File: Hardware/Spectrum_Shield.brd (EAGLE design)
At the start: 59.7 x 53.3 mm, 25 parts, among them IC1 MSGEQ7SOIC, IC2 MSGEQ7SOIC, U1 ARDUINO_R3_SHIELD

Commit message: computer change #2
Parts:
- removed JP1: LOGO-SFENEW, SparkFun:SFE-NEW-WEBLOGO
- added U$2: (no value), SparkFun-Aesthetics:SFE_LOGO_FLAME_.2
- C1, C2, C3, C4: device SparkFun:0402-CAP -> SparkFun-Capacitors:0603-CAP
- moved U$1 66.8 mm to (57.0, 8.13)
- moved JP5 31.9 mm to (57.1, 38.1)
- moved C5 8.98 mm to (44.5, 22.9), turned to 270 degrees
- moved IC2 7.62 mm to (35.6, 17.5)
- moved C6 6.48 mm to (41.9, 34.3), turned to 180 degrees
- moved IC1 5.68 mm to (35.6, 34.3)
- moved S1 5.60 mm to (47.9, 9.14)
- moved C2 5.55 mm to (36.6, 40.6)
- moved C8 5.39 mm to (33.0, 40.6)
- moved C3 5.19 mm to (41.9, 13.1)
- moved C7 5.09 mm to (34.5, 24.3)
- moved R2 5.04 mm to (34.8, 40.6)
- moved C1 5.04 mm to (41.9, 32.3)
- moved C4 4.95 mm to (38.5, 24.3)
- moved R1 4.30 mm to (36.6, 24.3)
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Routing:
- net VCC: track 25.1 -> 56.9 mm
- net ANALOG0: track 15.2 -> 38.2 mm, vias 2 -> 3
- net RIGHT: track 29.3 -> 45.8 mm
- net LEFT: track 16.7 -> 31.3 mm, vias 1 -> 0
- net RESET: track 37.7 -> 45.3 mm
- net N$5: track 4.43 -> 9.77 mm
- net STROBE: track 40.9 -> 45.6 mm
- net N$4: track 7.93 -> 12.2 mm
- net N$3: track 7.97 -> 11.2 mm
- net N$2: track 2.13 -> 5.24 mm
- net N$227: track 23.0 -> 25.8 mm
- net ANALOG1: track 19.1 -> 20.9 mm
- net N$6: track 4.64 -> 3.15 mm
- net N$1: track 2.13 -> 2.96 mm
- net N$7: track 1.57 -> 2.34 mm
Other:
- board text removed: "Spectrum Shield"

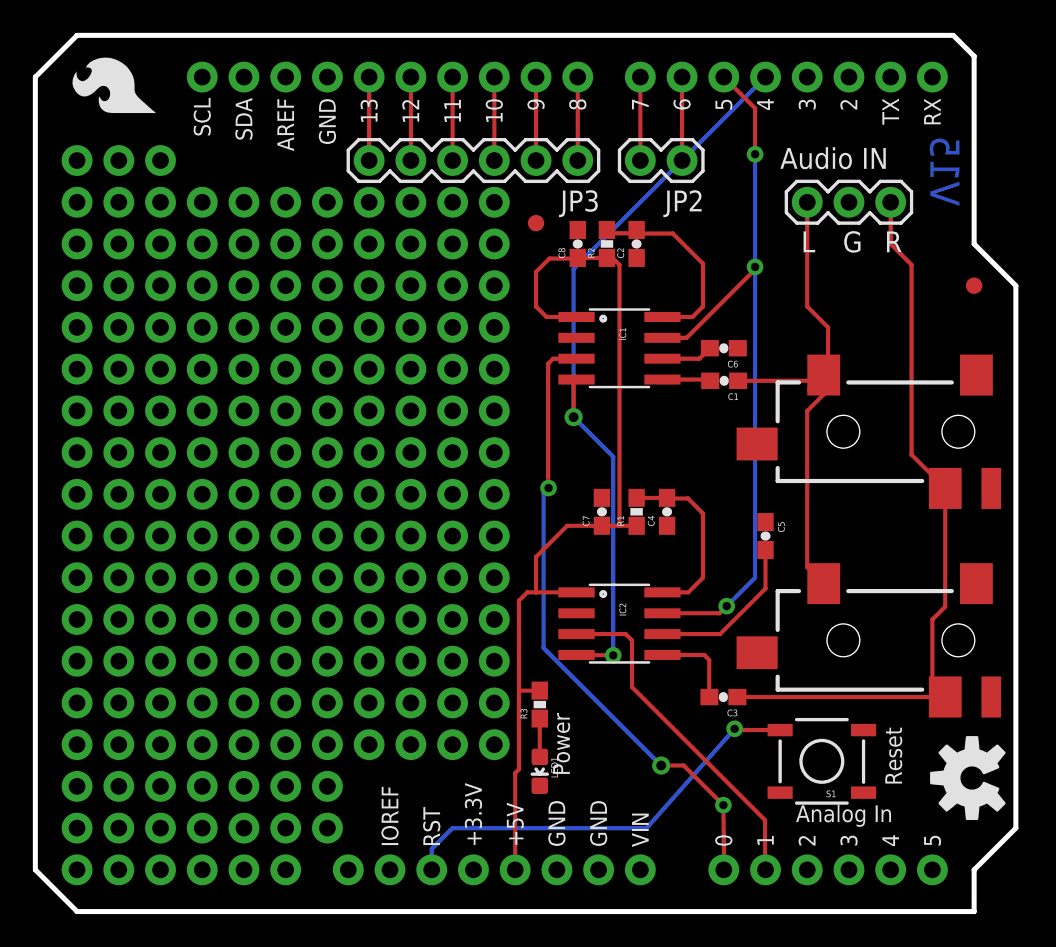
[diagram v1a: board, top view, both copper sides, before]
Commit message: Upd audiojk/0603/ trace re-routes
Updated the audio jack to smd, changed res/caps to 0603 as well as the
LED.  Added the OSHW logo and updated the shield to the R3.
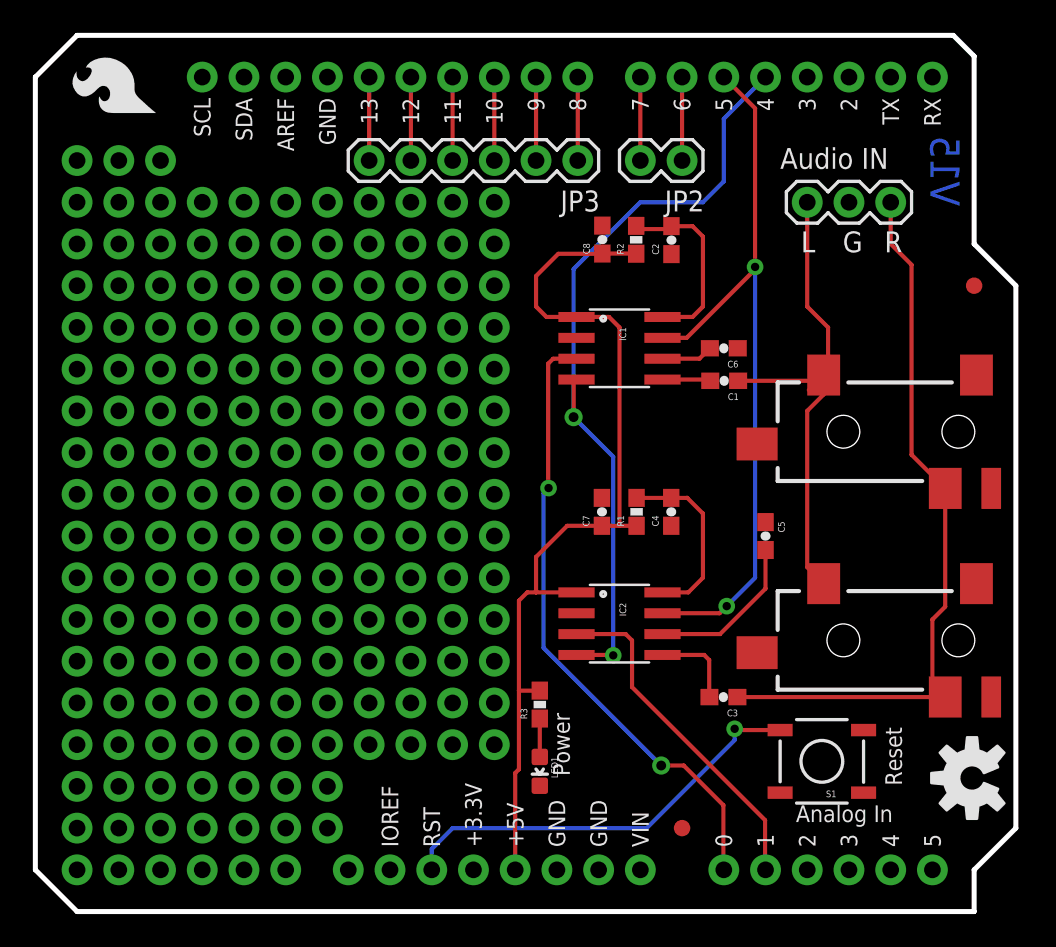
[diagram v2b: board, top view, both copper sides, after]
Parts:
- moved JP4 37.9 mm to (39.4, 5.08)
- moved C2 2.14 mm to (38.7, 40.9)
- moved R2 1.80 mm to (36.6, 40.9)
- moved C8 1.52 mm to (34.5, 40.9)
- moved C4 0.25 mm to (38.7, 24.3)
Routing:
- net STROBE: track 45.6 -> 47.9 mm
- net N$4: track 12.2 -> 11.5 mm
- net ANALOG0: track 38.2 -> 38.1 mm, vias 3 -> 2
- net RESET: vias 3 -> 2

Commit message: Trace Clean up.
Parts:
- moved JP4 17.3 mm to (56.6, 4.70)
- moved R3 2.59 mm to (33.2, 12.1)
- moved LED1 2.57 mm to (33.2, 8.92)
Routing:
- net STROBE: track 47.9 -> 45.6 mm
- net VCC: track 56.7 -> 58.0 mm
- net N$7: track 2.34 -> 1.45 mm
- net ANALOG0: track 38.1 -> 37.3 mm
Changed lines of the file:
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@@
 <setting verticaltext="up"/>
 </settings>
-<grid distance="0.05" unitdist="inch" unit="inch" style="lines" multiple="1" display="yes" altdistance="0.0001" altunitdist="inch" altunit="inch"/>
+<grid distance="0.05" unitdist="inch" unit="inch" style="lines" multiple="1" display="yes" altdistance="0.005" altunitdist="inch" altunit="inch"/>
 <layers>
 <layer number="1" name="Top" color="4" fill="1" visible="yes" active="yes"/>
@@
 <layer number="47" name="Measures" color="7" fill="1" visible="no" active="yes"/>
 <layer number="48" name="Document" color="7" fill="1" visible="no" active="yes"/>
-<layer number="49" name="Reference" color="7" fill="1" visible="yes" active="yes"/>
+<layer number="49" name="Reference" color="7" fill="1" visible="no" active="yes"/>
 <layer number="50" name="dxf" color="7" fill="1" visible="no" active="yes"/>
 <layer number="51" name="tDocu" color="6" fill="1" visible="yes" active="yes"/>
@@
 <wire x1="0" y1="2.54" x2="2.54" y2="0" width="0.3048" layer="20"/>
 <text x="33.274" y="40.386" size="2.1844" layer="22" font="vector" ratio="15" rot="MR270">bliptronics.com</text>
-<text x="35.179" y="37.211" size="1.27" layer="22" font="vector" ratio="15" rot="MR270">Based on design by</text>
+<text x="35.814" y="36.83" size="1.27" layer="22" font="vector" ratio="15" rot="MR270">Based on design by</text>
 <text x="45.339" y="45.212" size="1.27" layer="21" font="vector" ratio="15">Audio IN</text>
 <text x="46.609" y="40.132" size="1.27" layer="21" font="vector" ratio="15">L</text>
@@
 <text x="51.689" y="40.132" size="1.27" layer="21" font="vector" ratio="15">R</text>
 <text x="51.7398" y="11.2268" size="1.016" layer="21" font="vector" ratio="15" rot="R270">Reset</text>
-<text x="32.5374" y="8.255" size="1.016" layer="21" font="vector" ratio="15" rot="R90">Power</text>
-<text x="56.261" y="47.244" size="1.778" layer="16" font="vector" ratio="15" rot="MR270">V15</text>
+<text x="35.0774" y="8.255" size="1.016" layer="21" font="vector" ratio="15" rot="R90">Power</text>
+<text x="56.261" y="47.244" size="1.27" layer="16" font="vector" ratio="15" rot="MR270">V15</text>
 </plain>
 <attributes>
@@
 <element name="AUDIO_IN" library="SparkFun" package="1X03" value="JUMPER-3PTH" x="46.99" y="43.18" smashed="yes"/>
 <element name="U1" library="SparkFun-Boards" package="UNO_R3_SHIELD" value="ARDUINO_R3_SHIELD" x="0" y="53.34" rot="R270"/>
-<element name="R3" library="SparkFun-Resistors" package="0603-RES" value="330" x="30.7086" y="12.5984" rot="R90">
-<attribute name="PROD_ID" value="RES-00818" x="30.7086" y="12.5984" size="1.778" layer="27" rot="R90" display="off"/>
-<attribute name="VALUE" value="330" x="30.7086" y="12.5984" size="1.778" layer="27" rot="R90" display="off"/>
-</element>
-<element name="LED1" library="SparkFun-LED" package="LED-0603" value="RED" x="30.7086" y="8.5344" rot="R180">
-<attribute name="PROD_ID" value="DIO-00819" x="30.7086" y="8.5344" size="1.778" layer="27" rot="R180" display="off"/>
-<attribute name="VALUE" value="RED" x="30.7086" y="8.5344" size="1.778" layer="27" rot="R180" display="off"/>
+<element name="R3" library="SparkFun-Resistors" package="0603-RES" value="330" x="33.2486" y="12.0904" rot="R90">
+<attribute name="PROD_ID" value="RES-00818" x="33.2486" y="12.0904" size="1.778" layer="27" rot="R90" display="off"/>
+<attribute name="VALUE" value="330" x="33.2486" y="12.0904" size="1.778" layer="27" rot="R90" display="off"/>
+</element>
+<element name="LED1" library="SparkFun-LED" package="LED-0603" value="RED" x="33.2486" y="8.9154" rot="R180">
+<attribute name="PROD_ID" value="DIO-00819" x="33.2486" y="8.9154" size="1.778" layer="27" rot="R180" display="off"/>
+<attribute name="VALUE" value="RED" x="33.2486" y="8.9154" size="1.778" layer="27" rot="R180" display="off"/>
 </element>
 <element name="JP2" library="SparkFun" package="1X02" value="" x="39.37" y="45.72" rot="R180"/>
@@
 <element name="IC1" library="SparkFun" package="SOIC8" value="MSGEQ7SOIC" x="35.56" y="34.29" rot="R270"/>
 <element name="IC2" library="SparkFun" package="SOIC8" value="MSGEQ7SOIC" x="35.56" y="17.526" rot="R270"/>
-<element name="JP4" library="SparkFun" package="FIDUCIAL-1X2" value="FIDUCIAL1X2" x="39.37" y="5.08"/>
+<element name="JP4" library="SparkFun" package="FIDUCIAL-1X2" value="FIDUCIAL1X2" x="56.642" y="4.699"/>
 <element name="JP5" library="SparkFun" package="FIDUCIAL-1X2" value="FIDUCIAL1X2" x="57.15" y="38.1"/>
 <element name="U$1" library="SparkFun-Aesthetics" package="OSHW-LOGO-M" value="" x="57.023" y="8.128" rot="R90"/>
@@
 <wire x1="32.766" y1="30.099" x2="32.766" y2="32.2072" width="0.254" layer="1"/>
 <wire x1="32.766" y1="32.2072" x2="32.9438" y2="32.385" width="0.254" layer="1"/>
-<wire x1="32.766" y1="39.116" x2="32.766" y2="30.099" width="0.254" layer="16"/>
 <wire x1="32.766" y1="30.099" x2="35.179" y2="27.686" width="0.254" layer="16"/>
 <wire x1="35.179" y1="27.686" x2="35.179" y2="15.5956" width="0.254" layer="16"/>
 <wire x1="32.9438" y1="15.621" x2="35.1536" y2="15.621" width="0.254" layer="1"/>
 <wire x1="35.1536" y1="15.621" x2="35.179" y2="15.5956" width="0.254" layer="1"/>
-<wire x1="32.766" y1="39.116" x2="36.83" y2="43.18" width="0.254" layer="16"/>
-<wire x1="36.83" y1="43.18" x2="40.64" y2="43.18" width="0.254" layer="16"/>
-<wire x1="40.64" y1="43.18" x2="41.91" y2="44.45" width="0.254" layer="16"/>
-<wire x1="41.91" y1="44.45" x2="41.91" y2="48.26" width="0.254" layer="16"/>
-<wire x1="41.91" y1="48.26" x2="44.45" y2="50.8" width="0.254" layer="16"/>
+<wire x1="32.766" y1="30.099" x2="44.45" y2="41.783" width="0.254" layer="16"/>
+<wire x1="44.45" y1="41.783" x2="44.45" y2="50.8" width="0.254" layer="16"/>
 </signal>
 <signal name="N$1">
@@
 <contactref element="IC1" pad="1"/>
 <contactref element="IC2" pad="1"/>
-<wire x1="29.21" y1="2.54" x2="29.21" y2="8.4328" width="0.254" layer="1"/>
-<wire x1="29.21" y1="8.4328" x2="29.4386" y2="8.6614" width="0.254" layer="1"/>
 <wire x1="32.9438" y1="19.431" x2="30.48" y2="19.431" width="0.254" layer="1"/>
-<wire x1="30.48" y1="19.431" x2="29.9466" y2="19.431" width="0.254" layer="1"/>
-<wire x1="29.9466" y1="19.431" x2="29.4386" y2="18.923" width="0.254" layer="1"/>
 <wire x1="34.4932" y1="23.4832" x2="35.56" y2="23.4832" width="0.254" layer="1"/>
 <wire x1="35.56" y1="23.4832" x2="36.6014" y2="23.4832" width="0.254" layer="1"/>
@@
 <wire x1="32.3732" y1="23.4832" x2="30.48" y2="21.59" width="0.254" layer="1"/>
 <wire x1="30.48" y1="21.59" x2="30.48" y2="19.431" width="0.254" layer="1"/>
-<wire x1="29.4386" y1="8.6614" x2="29.4386" y2="13.4484" width="0.254" layer="1"/>
-<wire x1="29.4386" y1="13.4484" x2="29.4386" y2="18.923" width="0.254" layer="1"/>
-<wire x1="30.7086" y1="13.4484" x2="29.4386" y2="13.4484" width="0.254" layer="1"/>
 <wire x1="32.9438" y1="36.195" x2="31.115" y2="36.195" width="0.254" layer="1"/>
 <wire x1="31.115" y1="36.195" x2="30.48" y2="36.83" width="0.254" layer="1"/>
@@
 <wire x1="34.925" y1="36.195" x2="35.56" y2="35.56" width="0.254" layer="1"/>
 <wire x1="35.56" y1="35.56" x2="35.56" y2="23.4832" width="0.254" layer="1"/>
+<wire x1="29.21" y1="2.54" x2="30.48" y2="3.81" width="0.254" layer="1"/>
+<wire x1="30.48" y1="3.81" x2="30.48" y2="12.7" width="0.254" layer="1"/>
+<wire x1="30.48" y1="12.7" x2="30.48" y2="19.431" width="0.254" layer="1"/>
+<wire x1="33.2486" y1="12.9404" x2="33.0082" y2="12.7" width="0.254" layer="1"/>
+<wire x1="33.0082" y1="12.7" x2="30.48" y2="12.7" width="0.254" layer="1"/>
 </signal>
 <signal name="ANALOG0">
@@
 <wire x1="30.9372" y1="16.0528" x2="38.1" y2="8.89" width="0.254" layer="16"/>
 <via x="38.1" y="8.89" extent="1-16" drill="0.6"/>
-<wire x1="38.1" y1="8.89" x2="39.4716" y2="8.89" width="0.254" layer="1"/>
-<wire x1="39.4716" y1="8.89" x2="41.8846" y2="6.477" width="0.254" layer="1"/>
 <wire x1="32.9438" y1="33.655" x2="31.5214" y2="33.655" width="0.254" layer="1"/>
 <wire x1="31.5214" y1="33.655" x2="31.2166" y2="33.3502" width="0.254" layer="1"/>
 <wire x1="31.2166" y1="33.3502" x2="31.2166" y2="25.8064" width="0.254" layer="1"/>
 <wire x1="31.2166" y1="25.8064" x2="31.242" y2="25.781" width="0.254" layer="1"/>
-<wire x1="41.8846" y1="6.477" x2="41.8846" y2="2.5654" width="0.254" layer="1"/>
-<wire x1="41.8846" y1="2.5654" x2="41.91" y2="2.54" width="0.254" layer="1"/>
 <wire x1="30.9372" y1="16.0528" x2="30.9372" y2="25.4762" width="0.254" layer="16"/>
 <wire x1="30.9372" y1="25.4762" x2="31.242" y2="25.781" width="0.254" layer="16"/>
+<wire x1="38.1" y1="8.89" x2="41.91" y2="5.08" width="0.254" layer="1"/>
+<wire x1="41.91" y1="5.08" x2="41.91" y2="2.54" width="0.254" layer="1"/>
 </signal>
 <signal name="ANALOG1">
@@
 <contactref element="LED1" pad="A"/>
 <contactref element="R3" pad="1"/>
-<wire x1="30.7086" y1="9.4114" x2="30.7086" y2="11.7484" width="0.254" layer="1"/>
+<wire x1="33.2486" y1="9.7924" x2="33.2486" y2="11.2404" width="0.254" layer="1"/>
 </signal>
 <signal name="N$8">
